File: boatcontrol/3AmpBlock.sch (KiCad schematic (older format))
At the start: 12 parts, among them U1801 ULN2803A

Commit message: Restructure
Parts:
- added RN?: 4116R-1-103LF, DIP787W49P254L2197H469Q16N, symbol BoatControl:4116R-1-103LF
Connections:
- net labels added: MV3_AN_OFF_PULL, MV3_AN_ON_PULL, MV3_DIG_OFF_PULL, MV3_DIG_ON_PULL, MV4_AN_OFF_PULL, MV4_AN_ON_PULL, MV4_DIG_OFF_PULL, MV4_DIG_ON_PULL
- wire segments 130 -> 184
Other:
- note added: "Multivibrators to mux and clean up analogue and digital inputs\nPrevens energizing both coils in latching relays simultaneously and cleans up dirty signals."
- moved on the sheet: C301, C302, C303, C304, C305, C306, C307, C308, RN302

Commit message: More rewiring
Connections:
- net labels added: AN_OFF, AN_OFF_PULL, AN_ON, AN_ON_PULL, DIG_OFF, DIG_OFF_PULL, DIG_ON, DIG_ON_PULL, MUX_OFF, MUX_ON, R1, R2, RC1, RC2
- net labels removed: MV1_AN_OFF_PULL, MV1_AN_ON_PULL, MV1_DIG_OFF_PULL, MV1_DIG_ON_PULL, MV1_R1, MV1_R2, MV1_RC1, MV1_RC2, MV2_AN_OFF_PULL, MV2_AN_ON_PULL, MV2_DIG_OFF_PULL, MV2_DIG_ON_PULL, MV2_R1, MV2_R2, MV2_RC1, MV2_RC2, MV3_AN_OFF_PULL, MV3_AN_ON_PULL, MV3_DIG_OFF_PULL, MV3_DIG_ON_PULL, MV3_R1, MV3_R2, MV3_RC1, MV3_RC2, MV4_AN_OFF_PULL, MV4_AN_ON_PULL, MV4_DIG_OFF_PULL, MV4_DIG_ON_PULL, MV4_R1, MV4_R2, MV4_RC1, MV4_RC2
- wire segments 184 -> 251
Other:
- moved on the sheet: C301, C302, C303, C304, C305, C306, RN301, RN302, U301

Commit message: logig to dig name change
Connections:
- net labels removed: MUX_C1_OFF, MUX_C1_ON, MUX_C2_OFF, MUX_C2_ON, MUX_C3_OFF, MUX_C3_ON, MUX_C4_OFF, MUX_C4_ON
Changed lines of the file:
@@
 F0 "3AC1" 50
 F1 "3AmpCircuit.sch" 50
-F2 "ON_C?" B L 3050 1450 50
-F3 "OFF_C?" B L 3050 1600 50
-F4 "ON_LED_C?" I R 4050 1450 50
-F5 "OFF_LED_C?" I R 4050 1600 50
-F6 "OUT_C?" O R 4050 1950 50
-F7 "IN_C?" I L 3050 1950 50
+F2 "ON" B L 3050 1450 50
+F3 "OFF" B L 3050 1600 50
+F4 "ON_LED" I R 4050 1450 50
+F5 "OFF_LED" I R 4050 1600 50
+F6 "OUT" O R 4050 1950 50
+F7 "IN" I L 3050 1950 50
 $EndSheet
 $Sheet
@@
 F0 "3AC2" 50
 F1 "3AmpCircuit.sch" 50
-F2 "ON_C?" B L 3050 2350 50
-F3 "OFF_C?" B L 3050 2500 50
-F4 "ON_LED_C?" I R 4050 2350 50
-F5 "OFF_LED_C?" I R 4050 2500 50
-F6 "OUT_C?" O R 4050 2850 50
-F7 "IN_C?" I L 3050 2850 50
+F2 "ON" B L 3050 2350 50
+F3 "OFF" B L 3050 2500 50
+F4 "ON_LED" I R 4050 2350 50
+F5 "OFF_LED" I R 4050 2500 50
+F6 "OUT" O R 4050 2850 50
+F7 "IN" I L 3050 2850 50
 $EndSheet
 $Sheet
@@
 F0 "3AC3" 50
 F1 "3AmpCircuit.sch" 50
-F2 "ON_C?" B L 3050 3250 50
-F3 "OFF_C?" B L 3050 3400 50
-F4 "ON_LED_C?" I R 4050 3250 50
-F5 "OFF_LED_C?" I R 4050 3400 50
-F6 "OUT_C?" O R 4050 3750 50
-F7 "IN_C?" I L 3050 3750 50
+F2 "ON" B L 3050 3250 50
+F3 "OFF" B L 3050 3400 50
+F4 "ON_LED" I R 4050 3250 50
+F5 "OFF_LED" I R 4050 3400 50
+F6 "OUT" O R 4050 3750 50
+F7 "IN" I L 3050 3750 50
 $EndSheet
 $Sheet
@@
 F0 "3AC4" 50
 F1 "3AmpCircuit.sch" 50
-F2 "ON_C?" B L 3050 4150 50
-F3 "OFF_C?" B L 3050 4300 50
-F4 "ON_LED_C?" I R 4050 4150 50
-F5 "OFF_LED_C?" I R 4050 4300 50
-F6 "OUT_C?" O R 4050 4650 50
-F7 "IN_C?" I L 3050 4650 50
+F2 "ON" B L 3050 4150 50
+F3 "OFF" B L 3050 4300 50
+F4 "ON_LED" I R 4050 4150 50
+F5 "OFF_LED" I R 4050 4300 50
+F6 "OUT" O R 4050 4650 50
+F7 "IN" I L 3050 4650 50
 $EndSheet
 Wire Wire Line
@@
 	5350 2900 5450 2900
 Wire Wire Line
-	5450 2900 5450 2600
-Wire Wire Line
 	5450 900  1250 900
 Wire Wire Line
@@
 Wire Wire Line
 	1250 2900 1350 2900
-Wire Wire Line
-	5500 3000 5500 2550
 Wire Wire Line
 	5500 750  1200 750
@@
 Wire Wire Line
 	1350 4900 5350 4900
-Text HLabel 1200 750  0    50   Input ~ 0
-MUX_C2_OFF
-Text HLabel 1250 900  0    50   Input ~ 0
-MUX_C2_ON
-Text HLabel 1300 1050 0    50   Input ~ 0
-MUX_C1_OFF
-Text HLabel 1350 1200 0    50   Input ~ 0
-MUX_C1_ON
-Text HLabel 1350 4900 0    50   Input ~ 0
-MUX_C3_ON
-Text HLabel 1300 5050 0    50   Input ~ 0
-MUX_C3_OFF
-Text HLabel 1250 5200 0    50   Input ~ 0
-MUX_C4_ON
-Text HLabel 1200 5350 0    50   Input ~ 0
-MUX_C4_OFF
 Text Notes 9000 800  2    50   ~ 0
 Pull-up resistors for multivibrator inputs
@@
 	6000 3800 6100 3800
 Wire Wire Line
-	5450 2600 7200 2600
-Wire Wire Line
-	7200 2600 7200 3900
-Wire Wire Line
 	7200 3900 7350 3900
-Connection ~ 5450 2600
-Wire Wire Line
-	5450 2600 5450 900
 Wire Wire Line
 	7250 3800 7350 3800
@@
 	6000 2650 6000 3800
 Wire Wire Line
-	5500 2550 7250 2550
-Connection ~ 5500 2550
-Wire Wire Line
-	7250 2550 7250 3800
-Wire Wire Line
-	5500 750  5500 2550
+	5500 750  5500 2500
 Wire Wire Line
 	5500 3100 5750 3100
@@
 	9850 3900 9950 3900
 Connection ~ 5350 3400
+Wire Wire Line
+	5500 2500 7250 2500
+Connection ~ 5500 2500
+Wire Wire Line
+	5500 2500 5500 3000
+Wire Wire Line
+	7250 2500 7250 3800
+Wire Wire Line
+	5450 2550 7200 2550
+Connection ~ 5450 2550
+Wire Wire Line
+	5450 2550 5450 900
+Wire Wire Line
+	5450 2550 5450 2900
+Wire Wire Line
+	7200 2550 7200 3900
 $EndSCHEMATC

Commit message: Re-annotate after this
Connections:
- net labels added: DIG_ON_C1, DIG_ON_C2, DIG_ON_C3, DIG_ON_C4
- wire segments 251 -> 267
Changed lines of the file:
@@
 	4800 2500 4800 3000
-$Sheet
-S 7350 2750 900  1500
-U 5FDE25F0
-F0 "MultiVibratorAC2" 50
-F1 "MultiVibrator.sch" 50
-$EndSheet
 $Sheet
 S 8700 2750 900  1500
@@
 Text HLabel 9200 4250 1    50   Output ~ 0
 RC2
-Text HLabel 6600 3500 2    50   Input ~ 0
+Text HLabel 6650 3500 2    50   Input ~ 0
 DIG_OFF
 Wire Wire Line
@@
 Wire Wire Line
 	7300 4150 7300 5650
-Text HLabel 7850 3400 2    50   Input ~ 0
-DIG_ON
-Text HLabel 7850 3500 2    50   Input ~ 0
-DIG_OFF
-Text HLabel 9200 3400 2    50   Input ~ 0
-DIG_ON
-Text HLabel 9200 3500 2    50   Input ~ 0
-DIG_OFF
-Text HLabel 10450 3400 2    50   Input ~ 0
-DIG_ON
-Text HLabel 10450 3500 2    50   Input ~ 0
-DIG_OFF
-Text HLabel 7850 3600 2    50   Input ~ 0
-AN_ON
-Text HLabel 7850 3700 2    50   Input ~ 0
-AN_OFF
-Text HLabel 9200 3600 2    50   Input ~ 0
-AN_ON
-Text HLabel 9200 3700 2    50   Input ~ 0
-AN_OFF
-Text HLabel 10450 3600 2    50   Input ~ 0
-AN_ON
-Text HLabel 10450 3700 2    50   Input ~ 0
-AN_OFF
 Text HLabel 6100 3800 2    50   Input ~ 0
 MUX_ON
@@
 Text HLabel 9950 3900 2    50   Input ~ 0
 MUX_OFF
+Text HLabel 6650 3600 2    50   Input ~ 0
+AN_ON
+Text HLabel 6650 3700 2    50   Input ~ 0
+AN_OFF
+Text HLabel 6650 3400 2    50   Input ~ 0
+DIG_ON
+Connection ~ 6450 5750
+Wire Wire Line
+	8100 5850 8100 5750
+Wire Wire Line
+	6450 5750 8100 5750
+Wire Wire Line
+	8200 5700 8200 5850
+Wire Wire Line
+	7050 5700 8200 5700
+Wire Wire Line
+	8300 5650 8300 5850
+Wire Wire Line
+	7700 5650 8300 5650
+Wire Wire Line
+	8300 5600 8400 5600
+Wire Wire Line
+	8400 5600 8400 5850
+Connection ~ 8300 5600
+Wire Wire Line
+	8500 5600 8500 5850
+Wire Wire Line
+	8600 5650 8600 5850
+Wire Wire Line
+	8500 5600 8650 5600
+Connection ~ 8650 5600
+Wire Wire Line
+	8600 5650 9200 5650
+Wire Wire Line
+	8700 5700 8700 5850
+Wire Wire Line
+	8700 5700 9900 5700
+Wire Wire Line
+	8800 5750 8800 5850
+Wire Wire Line
+	8800 5750 10450 5750
+Wire Wire Line
+	7650 2000 7650 2750
+Wire Wire Line
+	7750 2000 7750 2750
+Wire Wire Line
+	7850 2000 7850 2750
+Wire Wire Line
+	7950 2000 7950 2750
+Wire Wire Line
+	9000 2000 9000 2750
+Wire Wire Line
+	9100 2000 9100 2750
+Wire Wire Line
+	9200 2000 9200 2750
+Wire Wire Line
+	9300 2000 9300 2750
+Wire Wire Line
+	7950 950  9000 950
+Connection ~ 9000 950
+Wire Wire Line
+	5350 2700 5950 2700
+Wire Wire Line
+	5950 2700 5950 3900
+Wire Wire Line
+	5950 3900 6100 3900
+Connection ~ 5350 2700
+Wire Wire Line
+	6000 3800 6100 3800
+Wire Wire Line
+	7200 3900 7350 3900
+Wire Wire Line
+	7250 3800 7350 3800
+Wire Wire Line
+	5400 2650 6000 2650
+Connection ~ 5400 2650
+Wire Wire Line
+	5400 2650 5400 1050
+Wire Wire Line
+	6000 2650 6000 3800
+Wire Wire Line
+	5500 750  5500 2500
+Wire Wire Line
+	5500 3100 5750 3100
+Wire Wire Line
+	5750 3100 5750 2200
+Wire Wire Line
+	5750 2200 8650 2200
+Wire Wire Line
+	8650 2200 8650 3800
+Wire Wire Line
+	8650 3800 8700 3800
+Connection ~ 5500 3100
+Wire Wire Line
+	5450 3200 5800 3200
+Wire Wire Line
+	5800 3200 5800 2250
+Wire Wire Line
+	5800 2250 8600 2250
+Wire Wire Line
+	8600 2250 8600 3900
+Wire Wire Line
+	8600 3900 8700 3900
+Connection ~ 5450 3200
+Wire Wire Line
+	5400 3300 5850 3300
+Wire Wire Line
+	5850 3300 5850 2350
+Wire Wire Line
+	5850 2350 9900 2350
+Wire Wire Line
+	9900 2350 9900 3800
+Wire Wire Line
+	9900 3800 9950 3800
+Connection ~ 5400 3300
+Wire Wire Line
+	5350 3400 5900 3400
+Wire Wire Line
+	5900 3400 5900 2400
+Wire Wire Line
+	5900 2400 9850 2400
+Wire Wire Line
+	9850 2400 9850 3900
+Wire Wire Line
+	9850 3900 9950 3900
+Connection ~ 5350 3400
+Wire Wire Line
+	5500 2500 7250 2500
+Connection ~ 5500 2500
+Wire Wire Line
+	5500 2500 5500 3000
+Wire Wire Line
+	7250 2500 7250 3800
+Wire Wire Line
+	5450 2550 7200 2550
+Connection ~ 5450 2550
+Wire Wire Line
+	5450 2550 5450 900
+Wire Wire Line
+	5450 2550 5450 2900
+Wire Wire Line
+	7200 2550 7200 3900
+Text HLabel 6600 3400 0    50   Output ~ 0
+DIG_ON_C1
+Wire Wire Line
+	6600 3400 6650 3400
+Text HLabel 6600 3500 0    50   Output ~ 0
+DIG_ON_C2
+Text HLabel 6600 3600 0    50   Output ~ 0
+DIG_ON_C3
+Text HLabel 6600 3700 0    50   Output ~ 0
+DIG_ON_C4
+Wire Wire Line
+	6600 3500 6650 3500
+Wire Wire Line
+	6600 3600 6650 3600
+Wire Wire Line
+	6600 3700 6650 3700
+$Sheet
+S 7350 2750 900  1500
+U 5FDE25F0
+F0 "MultiVibratorAC2" 50
+F1 "MultiVibrator.sch" 50
+$EndSheet
 $Sheet
 S 6100 2750 900  1500
@@
 F1 "MultiVibrator.sch" 50
 $EndSheet
-Text HLabel 6600 3600 2    50   Input ~ 0
+Text HLabel 7900 3500 2    50   Input ~ 0
+DIG_OFF
+Text HLabel 7900 3600 2    50   Input ~ 0
 AN_ON
-Text HLabel 6600 3700 2    50   Input ~ 0
+Text HLabel 7900 3700 2    50   Input ~ 0
 AN_OFF
-Text HLabel 6600 3400 2    50   Input ~ 0
+Text HLabel 7900 3400 2    50   Input ~ 0
 DIG_ON
-Connection ~ 6450 5750
-Wire Wire Line
-	8100 5850 8100 5750
-Wire Wire Line
-	6450 5750 8100 5750
-Wire Wire Line
-	8200 5700 8200 5850
-Wire Wire Line
-	7050 5700 8200 5700
-Wire Wire Line
-	8300 5650 8300 5850
-Wire Wire Line
-	7700 5650 8300 5650
-Wire Wire Line
-	8300 5600 8400 5600
-Wire Wire Line
-	8400 5600 8400 5850
-Connection ~ 8300 5600
-Wire Wire Line
-	8500 5600 8500 5850
-Wire Wire Line
-	8600 5650 8600 5850
-Wire Wire Line
-	8500 5600 8650 5600
-Connection ~ 8650 5600
-Wire Wire Line
-	8600 5650 9200 5650
-Wire Wire Line
-	8700 5700 8700 5850
-Wire Wire Line
-	8700 5700 9900 5700
-Wire Wire Line
-	8800 5750 8800 5850
-Wire Wire Line
-	8800 5750 10450 5750
-Wire Wire Line
-	7650 2000 7650 2750
-Wire Wire Line
-	7750 2000 7750 2750
-Wire Wire Line
-	7850 2000 7850 2750
-Wire Wire Line
-	7950 2000 7950 2750
-Wire Wire Line
-	9000 2000 9000 2750
-Wire Wire Line
-	9100 2000 9100 2750
-Wire Wire Line
-	9200 2000 9200 2750
-Wire Wire Line
-	9300 2000 9300 2750
-Wire Wire Line
-	7950 950  9000 950
-Connection ~ 9000 950
-Wire Wire Line
-	5350 2700 5950 2700
-Wire Wire Line
-	5950 2700 5950 3900
-Wire Wire Line
-	5950 3900 6100 3900
-Connection ~ 5350 2700
-Wire Wire Line
-	6000 3800 6100 3800
-Wire Wire Line
-	7200 3900 7350 3900
-Wire Wire Line
-	7250 3800 7350 3800
-Wire Wire Line
-	5400 2650 6000 2650
-Connection ~ 5400 2650
-Wire Wire Line
-	5400 2650 5400 1050
-Wire Wire Line
-	6000 2650 6000 3800
-Wire Wire Line
-	5500 750  5500 2500
-Wire Wire Line
-	5500 3100 5750 3100
-Wire Wire Line
-	5750 3100 5750 2200
-Wire Wire Line
-	5750 2200 8650 2200
-Wire Wire Line
-	8650 2200 8650 3800
-Wire Wire Line
-	8650 3800 8700 3800
-Connection ~ 5500 3100
-Wire Wire Line
-	5450 3200 5800 3200
-Wire Wire Line
-	5800 3200 5800 2250
-Wire Wire Line
-	5800 2250 8600 2250
-Wire Wire Line
-	8600 2250 8600 3900
-Wire Wire Line
-	8600 3900 8700 3900
-Connection ~ 5450 3200
-Wire Wire Line
-	5400 3300 5850 3300
-Wire Wire Line
-	5850 3300 5850 2350
-Wire Wire Line
-	5850 2350 9900 2350
-Wire Wire Line
-	9900 2350 9900 3800
-Wire Wire Line
-	9900 3800 9950 3800
-Connection ~ 5400 3300
-Wire Wire Line
-	5350 3400 5900 3400
-Wire Wire Line
-	5900 3400 5900 2400
-Wire Wire Line
-	5900 2400 9850 2400
-Wire Wire Line
-	9850 2400 9850 3900
-Wire Wire Line
-	9850 3900 9950 3900
-Connection ~ 5350 3400
-Wire Wire Line
-	5500 2500 7250 2500
-Connection ~ 5500 2500
-Wire Wire Line
-	5500 2500 5500 3000
-Wire Wire Line
-	7250 2500 7250 3800
-Wire Wire Line
-	5450 2550 7200 2550
-Connection ~ 5450 2550
-Wire Wire Line
-	5450 2550 5450 900
-Wire Wire Line
-	5450 2550 5450 2900
-Wire Wire Line
-	7200 2550 7200 3900
+Text HLabel 7850 3400 0    50   Output ~ 0
+DIG_ON_C1
+Wire Wire Line
+	7850 3400 7900 3400
+Text HLabel 7850 3500 0    50   Output ~ 0
+DIG_ON_C2
+Text HLabel 7850 3600 0    50   Output ~ 0
+DIG_ON_C3
+Text HLabel 7850 3700 0    50   Output ~ 0
+DIG_ON_C4
+Wire Wire Line
+	7850 3500 7900 3500
+Wire Wire Line
+	7850 3600 7900 3600
+Wire Wire Line
+	7850 3700 7900 3700
+Text HLabel 9250 3500 2    50   Input ~ 0
+DIG_OFF
+Text HLabel 9250 3600 2    50   Input ~ 0
+AN_ON
+Text HLabel 9250 3700 2    50   Input ~ 0
+AN_OFF
+Text HLabel 9250 3400 2    50   Input ~ 0
+DIG_ON
+Text HLabel 9200 3400 0    50   Output ~ 0
+DIG_ON_C1
+Wire Wire Line
+	9200 3400 9250 3400
+Text HLabel 9200 3500 0    50   Output ~ 0
+DIG_ON_C2
+Text HLabel 9200 3600 0    50   Output ~ 0
+DIG_ON_C3
+Text HLabel 9200 3700 0    50   Output ~ 0
+DIG_ON_C4
+Wire Wire Line
+	9200 3500 9250 3500
+Wire Wire Line
+	9200 3600 9250 3600
+Wire Wire Line
+	9200 3700 9250 3700
+Text HLabel 10500 3500 2    50   Input ~ 0
+DIG_OFF
+Text HLabel 10500 3600 2    50   Input ~ 0
+AN_ON
+Text HLabel 10500 3700 2    50   Input ~ 0
+AN_OFF
+Text HLabel 10500 3400 2    50   Input ~ 0
+DIG_ON
+Text HLabel 10450 3400 0    50   Output ~ 0
+DIG_ON_C1
+Wire Wire Line
+	10450 3400 10500 3400
+Text HLabel 10450 3500 0    50   Output ~ 0
+DIG_ON_C2
+Text HLabel 10450 3600 0    50   Output ~ 0
+DIG_ON_C3
+Text HLabel 10450 3700 0    50   Output ~ 0
+DIG_ON_C4
+Wire Wire Line
+	10450 3500 10500 3500
+Wire Wire Line
+	10450 3600 10500 3600
+Wire Wire Line
+	10450 3700 10500 3700
 $EndSCHEMATC

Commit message: Rewire AC stuffs
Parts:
- removed C1803, C1804, C1805, C1806, C1807, C1808: 107CKS016M 100UF, Capacitor_THT:CP_Radial_D5.0mm_P2.00mm, symbol Device:C_Small
- added C? (x6): 107CKS016M 100UF, Capacitor_THT:CP_Radial_D5.0mm_P2.00mm, symbol Device:C_Small
- gave numbers to parts that had none: 2
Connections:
- net labels added: AN_OFF_C1, AN_ON_C1, DIG_OFF_C1
- net labels removed: AN_OFF, AN_OFF_PULL, AN_ON, AN_ON_PULL, DIG_OFF, DIG_OFF_PULL, DIG_ON, DIG_ON_C2, DIG_ON_C3, DIG_ON_C4, DIG_ON_PULL, MUX_OFF, MUX_ON, R1, R2, RC1, RC2
- wire segments 267 -> 292
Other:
- note added: "Resistors for multivibrator pull-up and timer circuits for relay pulses.\nThese can be swapped for higher/lower values as needed for longer pulses or more noise resistance."
- note removed: "Pull-up resistors for multivibrator inputs"
- note removed: "Timer circuit to restrict relay signals to 0.8s"
- moved on the sheet: C301, C302, RN301, RN302, U301

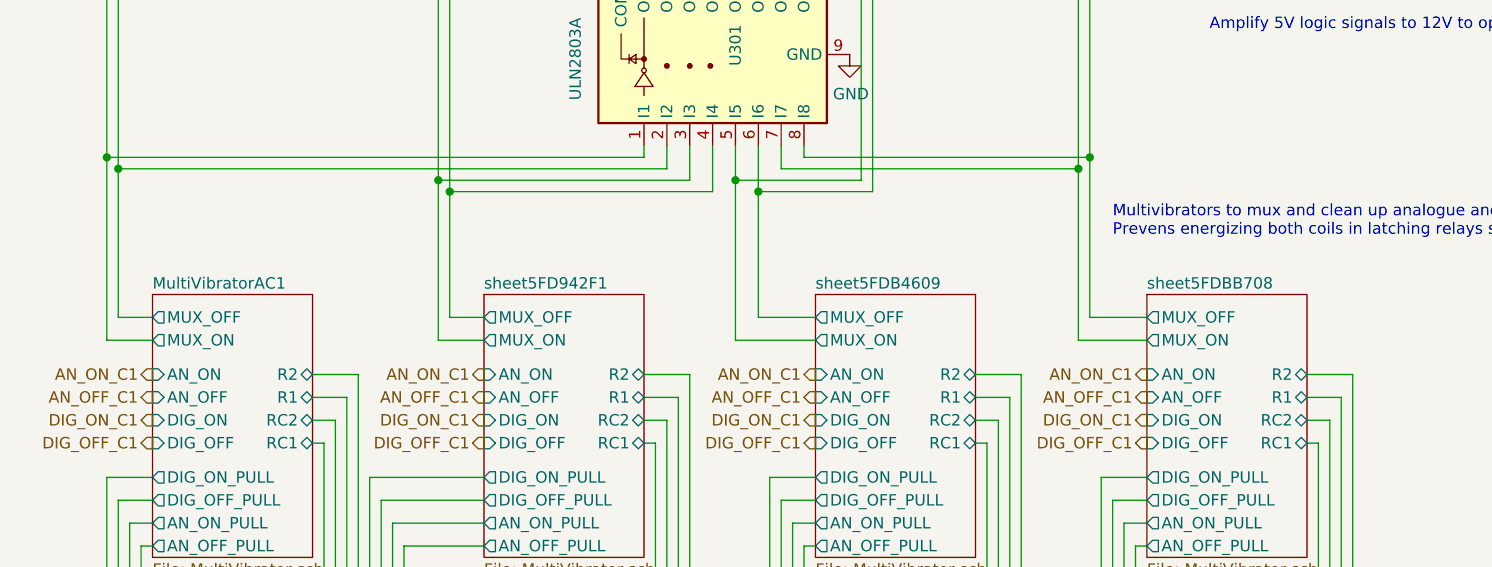
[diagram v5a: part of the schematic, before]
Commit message: Relabel multivibrators
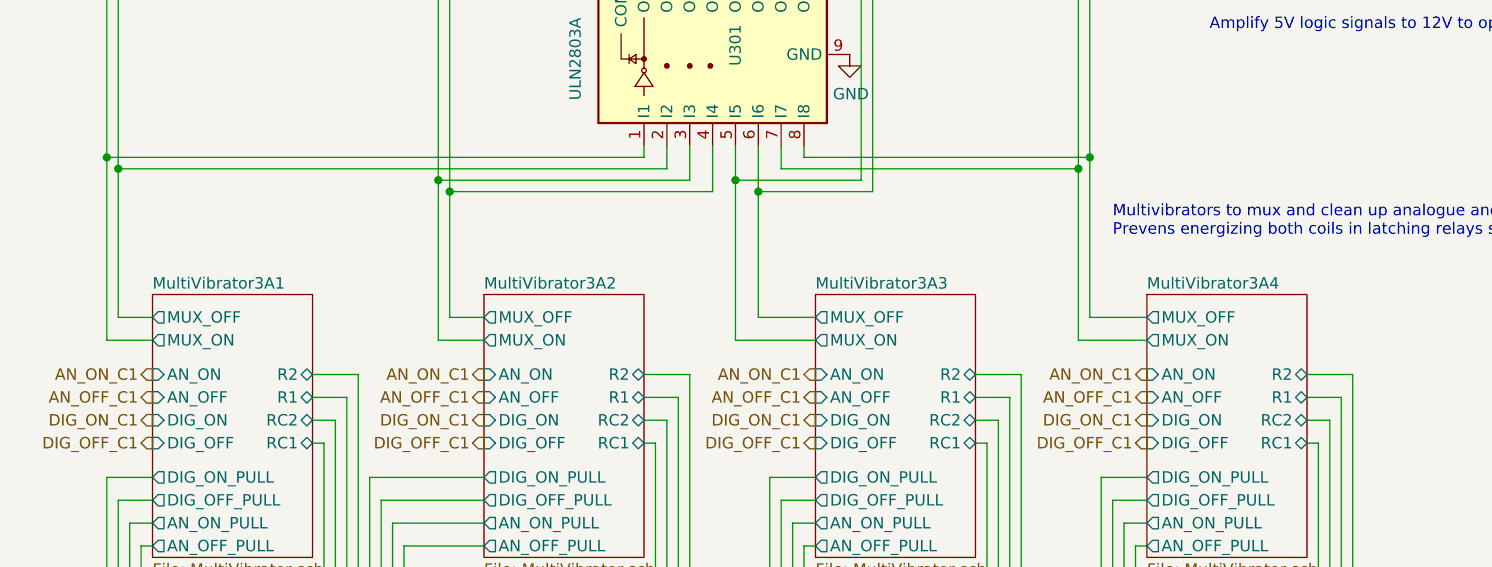
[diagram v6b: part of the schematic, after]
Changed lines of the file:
@@
 $Descr A4 11693 8268
 encoding utf-8
-Sheet 3 71
+Sheet 3 87
 Title "Boat Control Hat"
 Date "2020-07-09"
@@
 S 4200 4300 700  1150
 U 5FD94301
-F0 "sheet5FD942F1" 50
+F0 "MultiVibrator3A2" 50
 F1 "MultiVibrator.sch" 50
 F2 "DIG_OFF" I L 4200 4950 50
@@
 S 5650 4300 700  1150
 U 5FDB4619
-F0 "sheet5FDB4609" 50
+F0 "MultiVibrator3A3" 50
 F1 "MultiVibrator.sch" 50
 F2 "DIG_OFF" I L 5650 4950 50
@@
 S 2750 4300 700  1150
 U 5FC6571E
-F0 "MultiVibratorAC1" 50
+F0 "MultiVibrator3A1" 50
 F1 "MultiVibrator.sch" 50
 F2 "DIG_OFF" I L 2750 4950 50
@@
 S 7100 4300 700  1150
 U 5FDBB718
-F0 "sheet5FDBB708" 50
+F0 "MultiVibrator3A4" 50
 F1 "MultiVibrator.sch" 50
 F2 "DIG_OFF" I L 7100 4950 50

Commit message: Fix extra signals
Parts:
- gave numbers to parts that had none: 6
- renumbered C1801 to C3001, C1802 to C3002, RN1801 to RN3002, RN1802 to RN3003, RN304 to RN301, RN303 to RN304, U1801 to U3001
